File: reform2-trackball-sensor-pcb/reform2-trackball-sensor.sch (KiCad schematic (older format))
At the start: 14 parts, among them J1 Conn_01x06_Male, U1 PAT9125EL

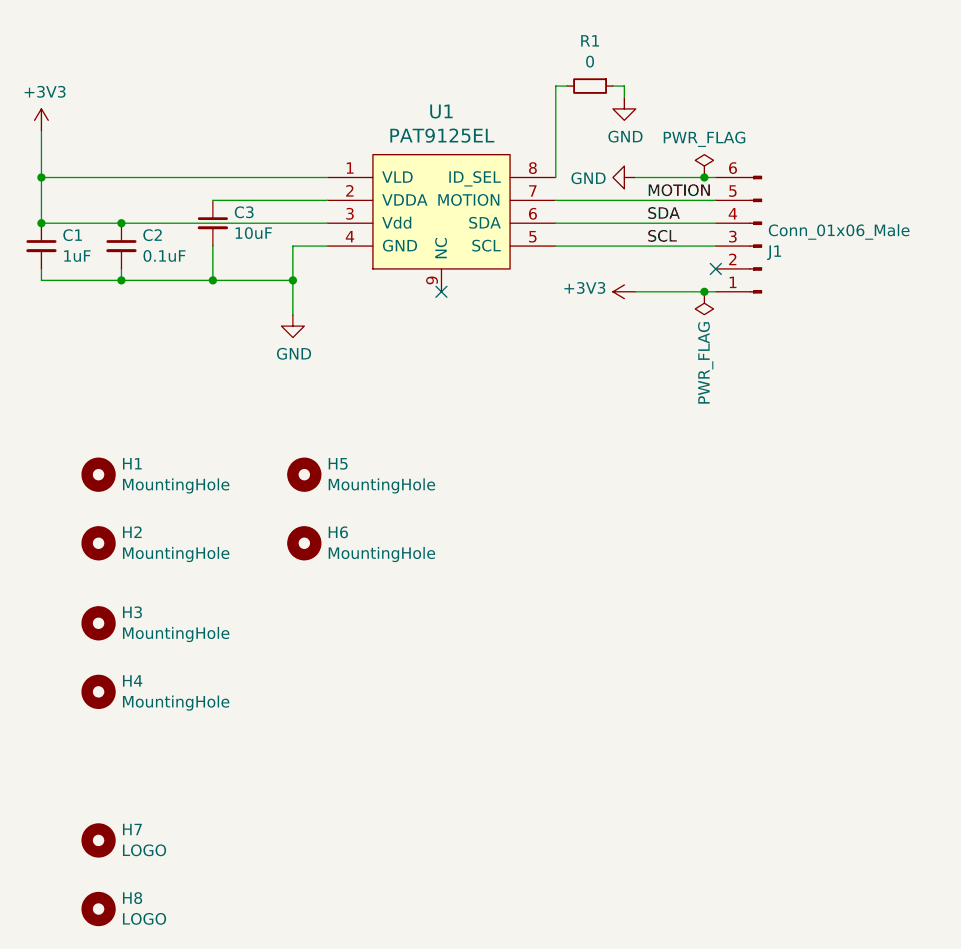
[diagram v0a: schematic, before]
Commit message: reform2: update PCBs incl. badges to production revs, add keyboard lettering, misc docs
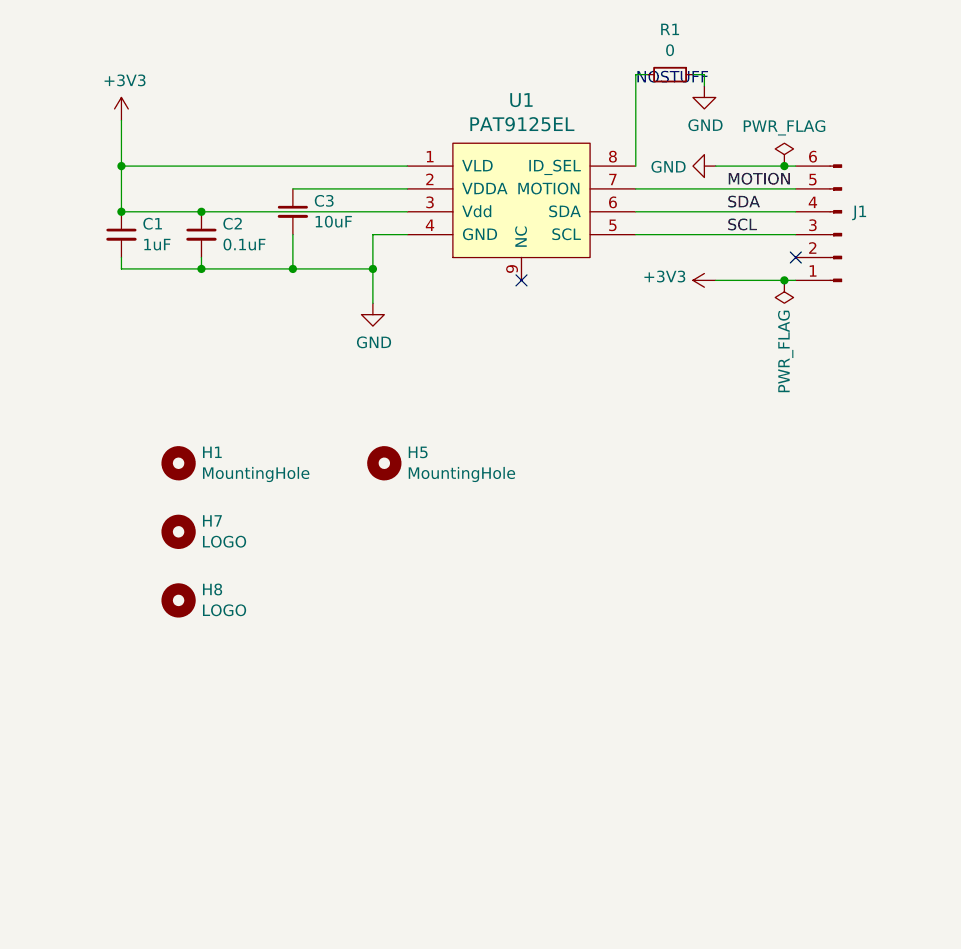
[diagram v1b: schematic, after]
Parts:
- removed H2, H3, H4, H6: MountingHole, MountingHole:MountingHole_2.2mm_M2, symbol Mechanical:MountingHole
- H8: footprint footprints:mnt-minilogo -> footprints-sensor:reform2-trackball-sensor-badge
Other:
- note added: "NOSTUFF"
- moved on the sheet: C1, C2, C3, H1, H5, H7, H8, J1, R1, U1
